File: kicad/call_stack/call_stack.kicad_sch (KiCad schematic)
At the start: 23 parts

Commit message: Completed design for call stack
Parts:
- added U24, U26, U27: ~, Package_DIP:DIP-14_W7.62mm, symbol custom_symbol_lib:dual_latch
- added U25: ~, Package_DIP:DIP-14_W7.62mm, symbol custom_symbol_lib:quad_OR
- U1: footprint Connector_PinHeader_2.54mm:PinHeader_1x23_P2.54mm_Vertical -> Connector_PinHeader_2.54mm:PinHeader_1x24_P2.54mm_Vertical
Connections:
- net at U23.3 (OUT): now also U1.24 (FAULT); no longer U1. (FAULT)
- net at U1.1 (V+), U8.20 (V+), U9.20 (V+): now also U10.16 (V+), U11.20 (V+), U2.16 (V+), U2.6 (B0), U21.14 (V+), U22.14 (V+), U3.20 (V+), U4.28 (V+), U5.28 (V+), U6.20 (V+), U7.20 (V+), U24.14 (V+), U25.14 (V+), U26.14 (V+), U27.14 (V+)
- net at U1.2 (GND), U8.10 (GND), U9.10 (GND): now also U10.8 (GND), U11.1 (OE#), U11.10 (GND), U12.2 (GND), U13.2 (GND), U14.2 (GND), U15.2 (GND), U16.2 (GND), U17.2 (GND), U18.2 (GND), U19.2 (GND), U2.7 (C_IN), U2.8 (GND), U20.2 (GND), U21.7 (GND), U22.7 (GND), U23.2 (GND), U3.1 (OE#), U3.10 (GND), U4.1 (A14), U4.14 (GND), U4.2 (A12), U4.20 (CE#), U4.21 (A10), U4.23 (A11), U4.24 (A9), U4.25 (A8), U4.26 (A13), U5.1 (A14), U5.14 (GND), U5.2 (A12), U5.20 (CE#), U5.21 (A10), U5.23 (A11), U5.24 (A9), U5.25 (A8), U5.26 (A13), U6.10 (GND), U7.10 (GND), U24.10 (1RESET), U24.4 (0RESET), U24.6 (0SET), U24.7 (GND), U24.8 (1SET), U25.12 (3A), U25.13 (3B), U25.5 (1A), U25.6 (1B), U25.7 (GND), U25.8 (2A), U25.9 (2B), U26.10 (1RESET), U26.4 (0RESET), U26.6 (0SET), U26.7 (GND), U26.8 (1SET), U27.10 (1RESET), U27.4 (0RESET), U27.6 (0SET), U27.7 (GND), U27.8 (1SET)
- net at U1.21 (A_CLK): now also U22.5 (2B), U26.11 (1CLK), U26.3 (0CLK), U27.11 (1CLK)
- net at U1.22 (B_CLK): now also U21.9 (I3), U24.11 (1CLK), U27.3 (0CLK); no longer U16.1 (IN)
- net at U1.3 (Push): now also U25.2 (0B), U27.9 (1D)
- net at U1.4 (Pop): now also U19.1 (IN), U24.5 (0D), U25.1 (0A), U26.5 (0D)
- net at U14.1 (IN): now also U22.4 (2A), U27.1 (0Q)
- net at U20.1 (IN): now also U22.6 (2Q)
- net at U15.1 (IN): now also U24.1 (0Q)
- net at U18.1 (IN): now also U24.13 (1Q)
- net at U21.8 (03): now also U24.3 (0CLK)
- net at U12.1 (IN): now also U26.1 (0Q)
- net at U13.1 (IN): now also U27.13 (1Q), U27.5 (0D)
- net at U17.1 (IN): now also U24.9 (1D), U26.13 (1Q)
- new net: U1.23 (OE), U16.1 (IN)
- new net: U25.3 (Q0), U26.9 (1D)
- no-connect marks 1 -> 10
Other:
- moved on the sheet: U10, U11, U12, U13, U14, U15, U16, U17, U18, U19, U2, U20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

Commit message: stuff
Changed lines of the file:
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@@
 		)
 		(property "Footprint" "Connector_PinHeader_2.54mm:PinHeader_1x24_P2.54mm_Vertical"
-			(at 329.184 123.444 0)
+			(at 329.184 125.73 0)
 			(effects
 				(font
@@
 		(fields_autoplaced yes)
 		(property "Reference" "U11"
-			(at 140.0459 73.66 0)
-			(effects
-				(font
-					(size 1.27 1.27)
-				)
-				(justify left)
-			)
-		)
-		(property "Value" "~"
-			(at 140.0459 76.2 0)
-			(effects
-				(font
-					(size 1.27 1.27)
-				)
-				(justify left)
+			(at 144.5581 73.66 0)
+			(effects
+				(font
+					(size 1.27 1.27)
+				)
+				(justify right)
+			)
+		)
+		(property "Value" "~"
+			(at 144.5581 76.2 0)
+			(effects
+				(font
+					(size 1.27 1.27)
+				)
+				(justify right)
 			)
 		)
@@
 		(fields_autoplaced yes)
 		(property "Reference" "U7"
-			(at 257.81 129.9562 90)
-			(effects
-				(font
-					(size 1.27 1.27)
-				)
-			)
-		)
-		(property "Value" "~"
-			(at 257.81 128.0511 90)
+			(at 279.4 121.3798 90)
+			(effects
+				(font
+					(size 1.27 1.27)
+				)
+			)
+		)
+		(property "Value" "~"
+			(at 279.4 123.2849 90)
 			(effects
 				(font
@@
 		(fields_autoplaced yes)
 		(property "Reference" "U2"
-			(at 170.5259 62.23 0)
-			(effects
-				(font
-					(size 1.27 1.27)
-				)
-				(justify left)
-			)
-		)
-		(property "Value" "~"
-			(at 170.5259 64.77 0)
-			(effects
-				(font
-					(size 1.27 1.27)
-				)
-				(justify left)
+			(at 175.7365 62.23 0)
+			(effects
+				(font
+					(size 1.27 1.27)
+				)
+				(justify right)
+			)
+		)
+		(property "Value" "~"
+			(at 175.7365 64.77 0)
+			(effects
+				(font
+					(size 1.27 1.27)
+				)
+				(justify right)
 			)
 		)
@@
 		(fields_autoplaced yes)
 		(property "Reference" "U3"
-			(at 214.9759 63.5 0)
-			(effects
-				(font
-					(size 1.27 1.27)
-				)
-				(justify left)
-			)
-		)
-		(property "Value" "~"
-			(at 214.9759 66.04 0)
-			(effects
-				(font
-					(size 1.27 1.27)
-				)
-				(justify left)
+			(at 219.4881 63.5 0)
+			(effects
+				(font
+					(size 1.27 1.27)
+				)
+				(justify right)
+			)
+		)
+		(property "Value" "~"
+			(at 219.4881 66.04 0)
+			(effects
+				(font
+					(size 1.27 1.27)
+				)
+				(justify right)
 			)
 		)
@@
 		(fields_autoplaced yes)
 		(property "Reference" "U5"
-			(at 254.9241 73.66 0)
+			(at 254.9241 45.72 0)
 			(effects
 				(font
@@
 		)
 		(property "Value" "~"
-			(at 254.9241 71.12 0)
+			(at 254.9241 48.26 0)
 			(effects
 				(font
@@
 		(fields_autoplaced yes)
 		(property "Reference" "U8"
-			(at 280.67 121.5038 90)
-			(effects
-				(font
-					(size 1.27 1.27)
-				)
-			)
-		)
-		(property "Value" "~"
-			(at 280.67 123.4089 90)
+			(at 302.26 121.5038 90)
+			(effects
+				(font
+					(size 1.27 1.27)
+				)
+			)
+		)
+		(property "Value" "~"
+			(at 302.26 123.4089 90)
 			(effects
 				(font
@@
 		(fields_autoplaced yes)
 		(property "Reference" "U10"
-			(at 189.5759 77.47 0)
-			(effects
-				(font
-					(size 1.27 1.27)
-				)
-				(justify left)
-			)
-		)
-		(property "Value" "~"
-			(at 189.5759 80.01 0)
-			(effects
-				(font
-					(size 1.27 1.27)
-				)
-				(justify left)
+			(at 194.7865 77.47 0)
+			(effects
+				(font
+					(size 1.27 1.27)
+				)
+				(justify right)
+			)
+		)
+		(property "Value" "~"
+			(at 194.7865 80.01 0)
+			(effects
+				(font
+					(size 1.27 1.27)
+				)
+				(justify right)
 			)
 		)
@@
 		(fields_autoplaced yes)
 		(property "Reference" "U9"
-			(at 280.67 85.5062 90)
-			(effects
-				(font
-					(size 1.27 1.27)
-				)
-			)
-		)
-		(property "Value" "~"
-			(at 280.67 83.6011 90)
+			(at 302.26 76.9298 90)
+			(effects
+				(font
+					(size 1.27 1.27)
+				)
+			)
+		)
+		(property "Value" "~"
+			(at 302.26 78.8349 90)
 			(effects
 				(font
@@
 		(fields_autoplaced yes)
 		(property "Reference" "U6"
-			(at 257.81 77.0538 90)
-			(effects
-				(font
-					(size 1.27 1.27)
-				)
-			)
-		)
-		(property "Value" "~"
-			(at 257.81 78.9589 90)
-			(effects
-				(font
+			(at 279.4 77.0538 90)
+			(effects
+				(font
+					(size 1.27 1.27)
+				)
+			)
+		)
+		(property "Value" "~"
+			(at 279.4 78.9589 90)
+			(effects
+				(font

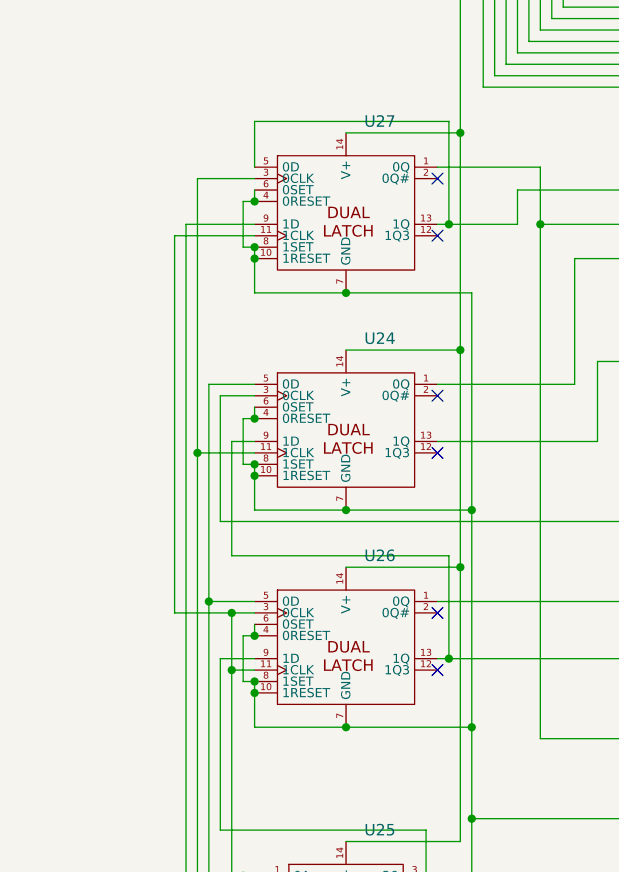
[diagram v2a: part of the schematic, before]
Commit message: Finished call stack schematic
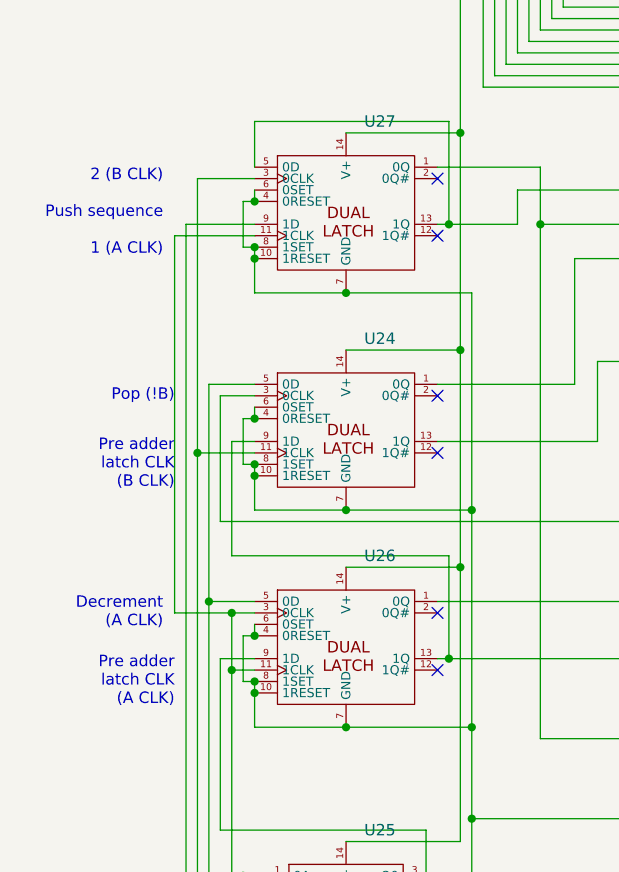
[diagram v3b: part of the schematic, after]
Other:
- note added: "2 (B CLK) Push sequence 1 (A CLK)"
- note added: "Decrement (A CLK)"
- note added: "Pop (!B)"
- note added: "Pre adder latch CLK (A CLK)"
- note added: "Pre adder latch CLK (B CLK)"
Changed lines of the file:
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@@
+		)
+	)
+	(text "Pre adder\nlatch CLK\n(B CLK)"
+		(exclude_from_sim no)
+		(at 87.63 151.13 0)
+		(effects
+			(font
+				(size 1.27 1.27)
+			)
+			(justify right)
+		)
+	)
+	(text "2 (B CLK)\n\nPush sequence\n\n1 (A CLK)"
+		(exclude_from_sim no)
+		(at 86.36 123.19 0)
+		(effects
+			(font
+				(size 1.27 1.27)
+			)
+			(justify right)
+		)
+	)
+	(text "Decrement\n(A CLK)"
+		(exclude_from_sim no)
+		(at 86.36 167.64 0)
+		(effects
+			(font
+				(size 1.27 1.27)
+			)
+			(justify right)
+		)
+	)
+	(text "Pop (!B)"
+		(exclude_from_sim no)
+		(at 87.63 143.51 0)
+		(effects
+			(font
+				(size 1.27 1.27)
+			)
+			(justify right)
+		)
+	)
+	(text "Pre adder\nlatch CLK\n(A CLK)"
+		(exclude_from_sim no)
+		(at 87.63 175.26 0)
+		(effects
+			(font
+				(size 1.27 1.27)
+			)
+			(justify right)
 		)
 	)
@@
 		)
 		(property "Footprint" "Package_DIP:DIP-20_W7.62mm"
-			(at 144.018 96.774 0)
-			(effects
-				(font
-					(size 1.27 1.27)
-				)
-				(hide yes)
-			)
-		)
-		(property "Datasheet" ""
-			(at 144.78 99.06 0)
+			(at 142.24 106.934 0)
+			(effects
+				(font
+					(size 1.27 1.27)
+				)
+				(hide yes)
+			)
+		)
+		(property "Datasheet" "https://toshiba.semicon-storage.com/info/TC74HC574AP_datasheet_en_20140301.pdf?did=16423&prodName=TC74HC574AP"
+			(at 142.494 109.22 0)
 			(effects
 				(font
@@
 		)
 		(property "Footprint" "Package_DIP:DIP-20_W7.62mm"
-			(at 257.556 123.952 0)
-			(effects
-				(font
-					(size 1.27 1.27)
-				)
-				(hide yes)
-			)
-		)
-		(property "Datasheet" ""
-			(at 255.27 123.19 0)
+			(at 247.396 125.73 0)
+			(effects
+				(font
+					(size 1.27 1.27)
+				)
+				(hide yes)
+			)
+		)
+		(property "Datasheet" "https://toshiba.semicon-storage.com/info/TC74HC574AP_datasheet_en_20140301.pdf?did=16423&prodName=TC74HC574AP"
+			(at 245.11 125.476 0)
 			(effects
 				(font
@@
 		)
 		(property "Footprint" "Package_DIP:DIP-16_W7.62mm"
-			(at 174.498 83.058 0)
-			(effects
-				(font
-					(size 1.27 1.27)
-				)
-				(hide yes)
-			)
-		)
-		(property "Datasheet" ""
-			(at 175.26 80.01 0)
+			(at 172.72 92.964 0)
+			(effects
+				(font
+					(size 1.27 1.27)
+				)
+				(hide yes)
+			)
+		)
+		(property "Datasheet" "https://www.ti.com/lit/ds/symlink/sn74f283.pdf?HQS=dis-dk-null-digikeymode-dsf-pf-null-wwe&ts=1723234691660&ref_url=https%253A%252F%252Fwww.ti.com%252Fgeneral%252Fdocs%252Fsuppproductinfo.tsp%253FdistId%253D10%2526gotoUrl%253Dhttps%253A%252F%252Fwww.ti.com%252Flit%252Fgpn%252Fsn74f283"
+			(at 172.72 95.504 0)
 			(effects
 				(font
@@
 		)
 		(property "Footprint" "Package_DIP:DIP-28_W15.24mm"
-			(at 251.714 160.02 0)
-			(effects
-				(font
-					(size 1.27 1.27)
-				)
-				(hide yes)
-			)
-		)
-		(property "Datasheet" ""
-			(at 248.92 163.83 0)
+			(at 252.984 170.688 0)
+			(effects
+				(font
+					(size 1.27 1.27)
+				)
+				(hide yes)
+			)
+		)
+		(property "Datasheet" "https://www.alliancememory.com/wp-content/uploads/pdf/AS6C62256.pdf"
+			(at 252.73 172.974 0)
 			(effects
 				(font
@@
 		)
 		(property "Footprint" "Package_DIP:DIP-20_W7.62mm"
-			(at 218.948 86.614 0)
-			(effects
-				(font
-					(size 1.27 1.27)
-				)
-				(hide yes)
-			)
-		)
-		(property "Datasheet" ""
-			(at 219.71 88.9 0)
+			(at 217.17 96.774 0)
+			(effects
+				(font
+					(size 1.27 1.27)
+				)
+				(hide yes)
+			)
+		)
+		(property "Datasheet" "https://toshiba.semicon-storage.com/info/TC74HC574AP_datasheet_en_20140301.pdf?did=16423&prodName=TC74HC574AP"
+			(at 217.424 99.06 0)
 			(effects
 				(font
@@
 		)
 		(property "Footprint" "Package_DIP:DIP-28_W15.24mm"
-			(at 251.714 46.99 0)
-			(effects
-				(font
-					(size 1.27 1.27)
-				)
-				(hide yes)
-			)
-		)
-		(property "Datasheet" ""
-			(at 248.92 43.18 0)
+			(at 252.984 36.322 0)
+			(effects
+				(font
+					(size 1.27 1.27)
+				)
+				(hide yes)
+			)
+		)
+		(property "Datasheet" "https://www.alliancememory.com/wp-content/uploads/pdf/AS6C62256.pdf"
+			(at 252.73 34.036 0)
 			(effects
 				(font
@@
 		)
 		(property "Footprint" "Package_DIP:DIP-20_W7.62mm"
-			(at 280.416 127.508 0)
-			(effects
-				(font
-					(size 1.27 1.27)
-				)
-				(hide yes)
-			)
-		)
-		(property "Datasheet" ""
-			(at 278.13 128.27 0)
+			(at 270.256 125.73 0)
+			(effects
+				(font
+					(size 1.27 1.27)
+				)
+				(hide yes)
+			)
+		)
+		(property "Datasheet" "https://toshiba.semicon-storage.com/info/TC74HC574AP_datasheet_en_20140301.pdf?did=16423&prodName=TC74HC574AP"
+			(at 267.97 125.984 0)
 			(effects
 				(font
@@
 		)
 		(property "Footprint" "Package_DIP:DIP-16_W7.62mm"
-			(at 193.548 98.298 0)
-			(effects
-				(font
-					(size 1.27 1.27)
-				)
-				(hide yes)
-			)
-		)
-		(property "Datasheet" ""
-			(at 194.31 95.25 0)
+			(at 191.77 108.204 0)
+			(effects
+				(font
+					(size 1.27 1.27)
+				)
+				(hide yes)
+			)
+		)
+		(property "Datasheet" "https://www.ti.com/lit/ds/symlink/sn74f283.pdf?HQS=dis-dk-null-digikeymode-dsf-pf-null-wwe&ts=1723234691660&ref_url=https%253A%252F%252Fwww.ti.com%252Fgeneral%252Fdocs%252Fsuppproductinfo.tsp%253FdistId%253D10%2526gotoUrl%253Dhttps%253A%252F%252Fwww.ti.com%252Flit%252Fgpn%252Fsn74f283"
+			(at 191.77 110.744 0)
 			(effects
 				(font
@@
 		)
 		(property "Footprint" "Package_DIP:DIP-14_W7.62mm"
-			(at 221.742 183.134 0)
-			(effects
-				(font
-					(size 1.27 1.27)
-				)
-				(hide yes)
-			)
-		)
-		(property "Datasheet" ""
-			(at 220.98 176.53 0)
+			(at 223.774 193.294 0)
+			(effects
+				(font
+					(size 1.27 1.27)
+				)
+				(hide yes)
+			)
+		)
+		(property "Datasheet" "https://mm.digikey.com/Volume0/opasdata/d220001/medias/docus/889/TC74HC04.pdf"
+			(at 223.52 195.58 0)
 			(effects
 				(font
@@
 		)
 		(property "Footprint" "Package_DIP:DIP-20_W7.62mm"
-			(at 280.416 79.502 0)
-			(effects
-				(font
-					(size 1.27 1.27)
-				)
-				(hide yes)
-			)
-		)
-		(property "Datasheet" ""
-			(at 278.13 78.74 0)
+			(at 270.256 81.28 0)
+			(effects
+				(font
+					(size 1.27 1.27)
+				)
+				(hide yes)
+			)
+		)
+		(property "Datasheet" "https://toshiba.semicon-storage.com/info/TC74HC574AP_datasheet_en_20140301.pdf?did=16423&prodName=TC74HC574AP"
+			(at 267.97 81.026 0)
 			(effects
 				(font
@@
 		)
 		(property "Footprint" "Package_DIP:DIP-14_W7.62mm"
-			(at 105.156 209.804 0)
-			(effects
-				(font
-					(size 1.27 1.27)
-				)
-				(hide yes)
-			)
-		)
-		(property "Datasheet" ""
-			(at 106.68 207.01 0)
+			(at 106.68 218.44 0)
+			(effects
+				(font
+					(size 1.27 1.27)
+				)
+				(hide yes)
+			)
+		)
+		(property "Datasheet" "https://www.jameco.com/Jameco/Products/ProdDS/13274.pdf"
+			(at 106.68 220.726 0)
 			(effects
 				(font
@@
 		)
 		(property "Footprint" "Package_DIP:DIP-14_W7.62mm"
-			(at 193.802 190.754 0)
-			(effects
-				(font
-					(size 1.27 1.27)
-				)
-				(hide yes)
-			)
-		)
-		(property "Datasheet" ""
-			(at 196.85 181.61 0)
+			(at 195.834 201.422 0)
+			(effects
+				(font
+					(size 1.27 1.27)
+				)
+				(hide yes)
+			)
+		)
+		(property "Datasheet" "https://toshiba.semicon-storage.com/info/TC74HC08AP_datasheet_en_20140301.pdf?did=7565&prodName=TC74HC08AP"
+			(at 195.58 203.708 0)
 			(effects
 				(font
@@
 		)
 		(property "Footprint" "Package_DIP:DIP-20_W7.62mm"
-			(at 257.556 83.058 0)
-			(effects
-				(font
-					(size 1.27 1.27)
-				)
-				(hide yes)
-			)
-		)
-		(property "Datasheet" ""
-			(at 255.27 83.82 0)
-			(effects
-				(font
+			(at 247.396 81.28 0)
+			(effects
+				(font
+					(size 1.27 1.27)
+				)
+				(hide yes)
+			)
+		)
+		(property "Datasheet" "https://toshiba.semicon-storage.com/info/TC74HC574AP_datasheet_en_20140301.pdf?did=16423&prodName=TC74HC574AP"
+			(at 245.11 81.534 0)
+			(effects
+				(font
